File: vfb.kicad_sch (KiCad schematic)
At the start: 12 parts, among them U6 OPA350UA

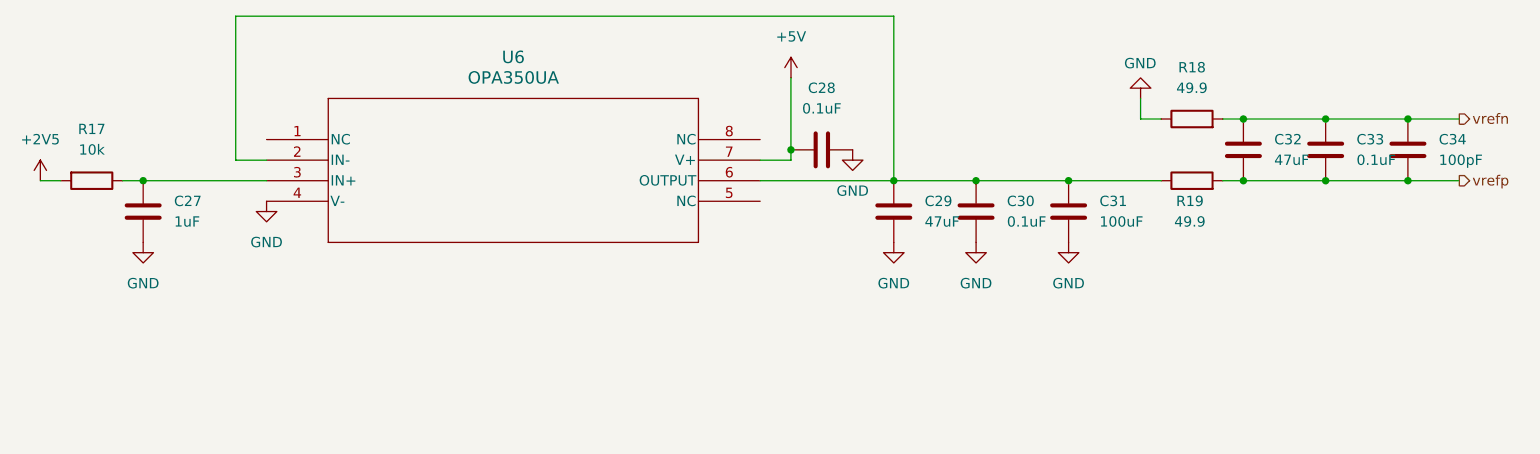
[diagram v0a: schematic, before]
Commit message: substituição do buffer de tensão com opa350 pela referencia de tensão ADR441xRZ
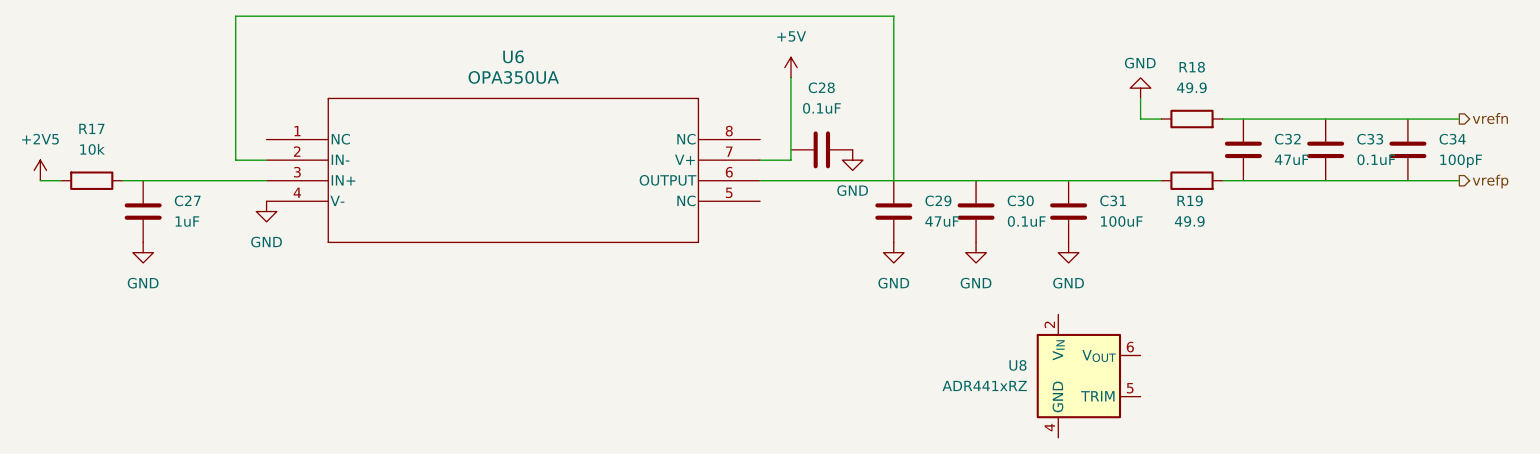
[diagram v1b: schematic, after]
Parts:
- added U8: ADR441xRZ, Package_SO:SOIC-8_3.9x4.9mm_P1.27mm, symbol Reference_Voltage:ADR441xRZ
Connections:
- net +5V: no longer C28.1
- net vrefn: no longer C32.1, C33.1, C34.1
- net vrefp: no longer C32.2, C33.2, C34.2
- net at R17.1, U6.3 (IN+): no longer C27.2
- new net: C29.1, U6.2 (IN-)
- new net: R19.1, U6.6 (OUTPUT)
- now unconnected: C30.1, C31.1
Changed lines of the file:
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@@
 	(generator_version "8.99")
 	(paper "A4")
-	(junction
-		(at 222.25 104.14)
-		(diameter 0)
-		(color 0 0 0 0)
-	)
-	(junction
-		(at 242.57 96.52)
-		(diameter 0)
-		(color 0 0 0 0)
-	)
-	(junction
-		(at 200.66 104.14)
-		(diameter 0)
-		(color 0 0 0 0)
-	)
-	(junction
-		(at 242.57 104.14)
-		(diameter 0)
-		(color 0 0 0 0)
-	)
-	(junction
-		(at 86.36 104.14)
-		(diameter 0)
-		(color 0 0 0 0)
-	)
-	(junction
-		(at 222.25 96.52)
-		(diameter 0)
-		(color 0 0 0 0)
-	)
-	(junction
-		(at 189.23 104.14)
-		(diameter 0)
-		(color 0 0 0 0)
-	)
-	(junction
-		(at 166.37 100.33)
-		(diameter 0)
-		(color 0 0 0 0)
-	)
-	(junction
-		(at 179.07 104.14)
-		(diameter 0)
-		(color 0 0 0 0)
-	)
-	(junction
-		(at 232.41 96.52)
-		(diameter 0)
-		(color 0 0 0 0)
-	)
-	(junction
-		(at 232.41 104.14)
-		(diameter 0)
-		(color 0 0 0 0)
-	)
 	(wire
 		(pts
-			(xy 219.71 104.14) (xy 222.25 104.14)
+			(xy 219.71 104.14) (xy 248.92 104.14)
 		)
 		(stroke
@@
 	(wire
 		(pts
-			(xy 222.25 96.52) (xy 219.71 96.52)
+			(xy 219.71 96.52) (xy 248.92 96.52)
 		)
 		(stroke
@@
 	(wire
 		(pts
-			(xy 162.56 104.14) (xy 179.07 104.14)
+			(xy 162.56 104.14) (xy 212.09 104.14)
 		)
 		(stroke
@@
 	(wire
 		(pts
-			(xy 242.57 96.52) (xy 232.41 96.52)
+			(xy 97.79 83.82) (xy 179.07 83.82)
 		)
 		(stroke
@@
 	(wire
 		(pts
-			(xy 97.79 83.82) (xy 179.07 83.82)
+			(xy 166.37 91.44) (xy 166.37 101.6)
 		)
 		(stroke
@@
 	(wire
 		(pts
-			(xy 166.37 100.33) (xy 166.37 91.44)
+			(xy 209.55 96.52) (xy 212.09 96.52)
 		)
 		(stroke
@@
 	(wire
 		(pts
-			(xy 86.36 104.14) (xy 101.6 104.14)
+			(xy 101.6 101.6) (xy 97.79 101.6)
 		)
 		(stroke
@@
 	(wire
 		(pts
-			(xy 232.41 96.52) (xy 222.25 96.52)
+			(xy 73.66 104.14) (xy 76.2 104.14)
 		)
 		(stroke
@@
 	(wire
 		(pts
-			(xy 166.37 101.6) (xy 166.37 100.33)
+			(xy 162.56 101.6) (xy 166.37 101.6)
 		)
 		(stroke
@@
 	(wire
 		(pts
-			(xy 242.57 104.14) (xy 248.92 104.14)
+			(xy 209.55 93.98) (xy 209.55 96.52)
 		)
 		(stroke
@@
 	(wire
 		(pts
-			(xy 209.55 96.52) (xy 212.09 96.52)
+			(xy 83.82 104.14) (xy 101.6 104.14)
 		)
 		(stroke
@@
 		)
 	)
-	(wire
-		(pts
-			(xy 189.23 104.14) (xy 200.66 104.14)
-		)
-		(stroke
-			(width 0)
-			(type default)
-		)
-	)
-	(wire
-		(pts
-			(xy 101.6 101.6) (xy 97.79 101.6)
-		)
-		(stroke
-			(width 0)
-			(type default)
-		)
-	)
-	(wire
-		(pts
-			(xy 232.41 104.14) (xy 242.57 104.14)
-		)
-		(stroke
-			(width 0)
-			(type default)
-		)
-	)
-	(wire
-		(pts
-			(xy 200.66 104.14) (xy 212.09 104.14)
-		)
-		(stroke
-			(width 0)
-			(type default)
-		)
-	)
-	(wire
-		(pts
-			(xy 242.57 96.52) (xy 248.92 96.52)
-		)
-		(stroke
-			(width 0)
-			(type default)
-		)
-	)
-	(wire
-		(pts
-			(xy 73.66 104.14) (xy 76.2 104.14)
-		)
-		(stroke
-			(width 0)
-			(type default)
-		)
-	)
-	(wire
-		(pts
-			(xy 162.56 101.6) (xy 166.37 101.6)
-		)
-		(stroke
-			(width 0)
-			(type default)
-		)
-	)
-	(wire
-		(pts
-			(xy 209.55 93.98) (xy 209.55 96.52)
-		)
-		(stroke
-			(width 0)
-			(type default)
-		)
-	)
-	(wire
-		(pts
-			(xy 222.25 104.14) (xy 232.41 104.14)
-		)
-		(stroke
-			(width 0)
-			(type default)
-		)
-	)
-	(wire
-		(pts
-			(xy 83.82 104.14) (xy 86.36 104.14)
-		)
-		(stroke
-			(width 0)
-			(type default)
-		)
-	)
-	(wire
-		(pts
-			(xy 179.07 104.14) (xy 189.23 104.14)
-		)
-		(stroke
-			(width 0)
-			(type default)
-		)
-	)
 	(hierarchical_label "vrefn"
 		(shape output)
@@
 					(unit 1)
 				)
+			)
+		)
+	)
+	(symbol
+		(lib_id "Reference_Voltage:ADR441xRZ")
+		(at 201.93 128.27 0)
+		(unit 1)
+		(exclude_from_sim no)
+		(in_bom yes)
+		(on_board yes)
+		(dnp no)
+		(fields_autoplaced yes)
+		(property "Reference" "U8"
+			(at 195.58 126.9999 0)
+			(effects
+				(font
+					(size 1.27 1.27)
+				)
+				(justify right)
+			)
+		)
+		(property "Value" "ADR441xRZ"
+			(at 195.58 129.5399 0)
+			(effects
+				(font
+					(size 1.27 1.27)
+				)
+				(justify right)
+			)
+		)
+		(property "Footprint" "Package_SO:SOIC-8_3.9x4.9mm_P1.27mm"
+			(at 224.282 142.748 0)
+			(effects
+				(font
+					(size 1.27 1.27)
+				)
+				(hide yes)
+			)
+		)
+		(property "Datasheet" "https://www.analog.com/media/en/technical-documentation/data-sheets/adr440_441_443_444_445.pdf"
+			(at 255.524 140.208 0)
+			(effects
+				(font
+					(size 1.27 1.27)
+				)
+				(hide yes)
+			)
+		)
+		(property "Description" "2.5V Voltage Reference, Ultraprecision, Low Noise, SOIC-8"
+			(at 232.664 137.922 0)
+			(effects
+				(font
+					(size 1.27 1.27)
+				)
+				(hide yes)
+			)
+		)
+		(pin "8"
+		)
+		(pin "6"
+		)
+		(pin "3"
+		)
+		(pin "4"
+		)
+		(pin "5"
+		)
+		(pin "7"
+		)
+		(pin "1"
+		)
+		(pin "2"
+		)
+		(instances
+			(project "esp32_ads1256"
+				(path "/dbf90267-57f9-4f5a-8904-b91a6fafdaf7/fd27ffa8-08fc-490f-b171-3a7361bbf7dd"
+					(reference "U8")
+					(unit 1)
+				)
